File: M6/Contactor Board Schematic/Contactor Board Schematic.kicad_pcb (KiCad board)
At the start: 2 copper layers, 52.1 x 42.7 mm, 8 parts

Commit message: CT board progress
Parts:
- removed the J_EXT4 at (128.0, 112.0)
- added D2: SMCJ28A, Diode_SMD:D_SMC, F.Cu at (116.8, 113.0)
- added D4: SMCJ28A, Diode_SMD:D_SMC, F.Cu at (105.4, 105.4)
- added D5: SMCJ28CA, Diode_SMD:D_SMC, F.Cu at (105.4, 83.6)
- added D6: SMCJ28CA, Diode_SMD:D_SMC, F.Cu at (139.7, 115.6)
- added U1: 12V Buck, Converter_DCDC:Converter_DCDC_TRACO_TSR-1_THT, F.Cu at (125.8, 115.6)
- J_EXT1: footprint Connector_AMASS:AMASS_XT30PW-F_1x02_P2.50mm_Horizontal -> TerminalBlock:TerminalBlock_MaiXu_MX126-5.0-02P_1x02_P5.00mm
- J_EXT2: renamed from J_EXT5; footprint Connector_AMASS:AMASS_XT30PW-F_1x02_P2.50mm_Horizontal -> Connector_AMASS:AMASS_XT30U-M_1x02_P5.0mm_Vertical
- J_EXT3: renamed from J_EXT2; footprint Connector_AMASS:AMASS_XT30PW-F_1x02_P2.50mm_Horizontal -> Connector_AMASS:AMASS_XT30U-M_1x02_P5.0mm_Vertical
- J_EXT4: renamed from J_EXT3; footprint Connector_AMASS:AMASS_XT30PW-F_1x02_P2.50mm_Horizontal -> Connector_AMASS:AMASS_XT30U-M_1x02_P5.0mm_Vertical
- moved J_EXT1 7.52 mm to (105.4, 97.7)
- moved J_EXT2 7.33 mm to (108.5, 112.4), turned to 180 degrees
- moved J_EXT4 2.59 mm to (146.1, 98.4)
- moved J_EXT3 2.49 mm to (146.1, 87.0)
- renumbered F3 to F1
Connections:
- net /To Contactor renamed /Contactor
- J_EXT2 pad 2: /From Switch -> /Switch
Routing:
- net /Switch: track 0.00 -> 34.1 mm
- net /From Switch: track 19.8 -> 0.00 mm, vias 1 -> 0
- net /Battery +: track 19.4 -> 0.00 mm
- net /Contactor: track 36.4 -> 44.3 mm, vias 2 -> 0
- net GND: track 0.21 -> 6.69 mm
- net Net-(D2-K): track 34.3 -> 39.7 mm
- net Net-(Contactor1-Pad2): track 3.90 -> 2.70 mm
- added copper zone on B.Cu, net /Battery +
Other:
- board text added: "Main Board"
- board text added: "Motor"

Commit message: Contactor Progress
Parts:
- added H1: MountingHole_Pad, MountingHole:MountingHole_2.7mm_Pad, F.Cu at (87.4, 88.1)
- added H2: MountingHole_Pad, MountingHole:MountingHole_2.7mm_Pad, F.Cu at (87.4, 95.0)
- added H3: MountingHole_Pad, MountingHole:MountingHole_2.7mm_Pad, F.Cu at (87.4, 102.0)
- added H4: MountingHole_Pad, MountingHole:MountingHole_2.7mm_Pad, F.Cu at (87.4, 108.9)
- moved D6 1.90 mm to (139.7, 113.7)
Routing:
- net /Battery +: track 0.00 -> 11.5 mm

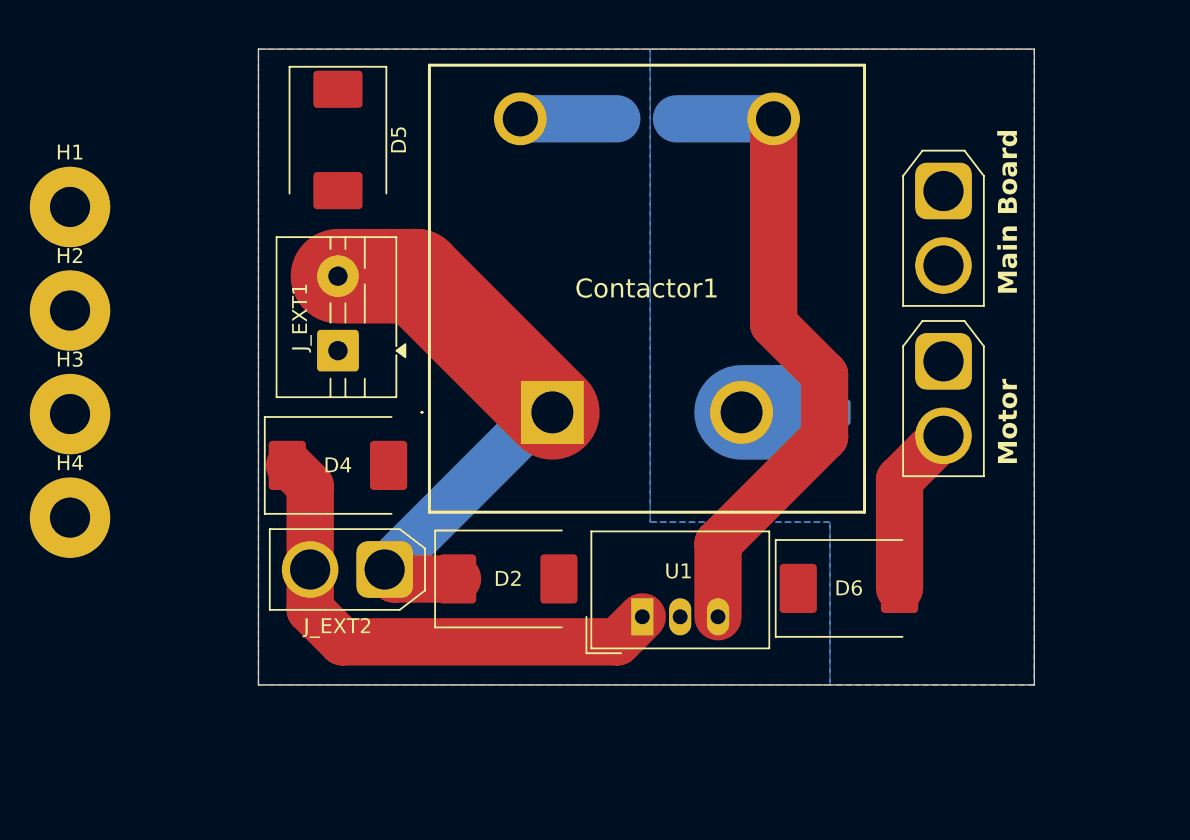
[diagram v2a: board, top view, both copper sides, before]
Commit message: XT60 connector for battery
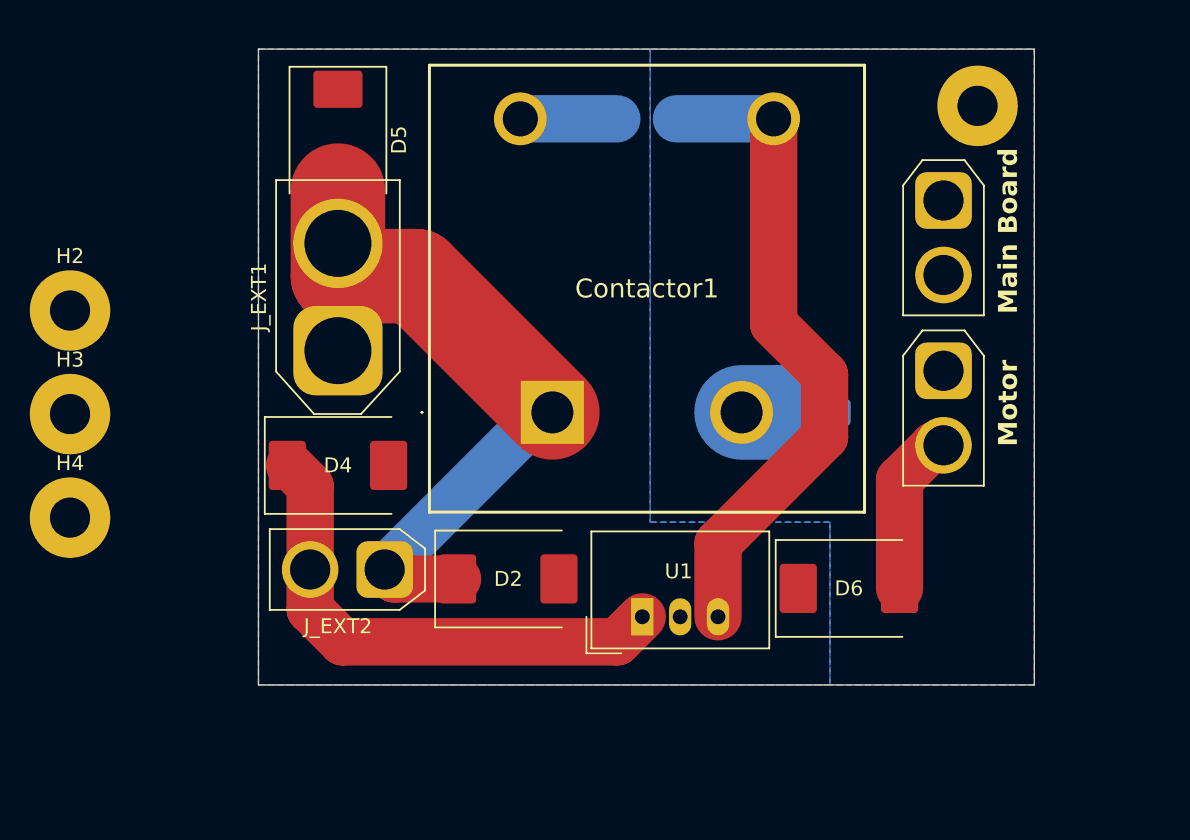
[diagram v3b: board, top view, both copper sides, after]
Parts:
- J_EXT1: footprint TerminalBlock:TerminalBlock_MaiXu_MX126-5.0-02P_1x02_P5.00mm -> Connector_AMASS:AMASS_XT60-M_1x02_P7.20mm_Vertical
- moved H1 61.3 mm to (148.3, 81.3)
- moved J_EXT4 0.64 mm to (146.1, 99.1)
- moved J_EXT3 0.63 mm to (146.1, 87.6)
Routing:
- net Net-(D2-K): track 39.7 -> 45.4 mm

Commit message: Finished contactor
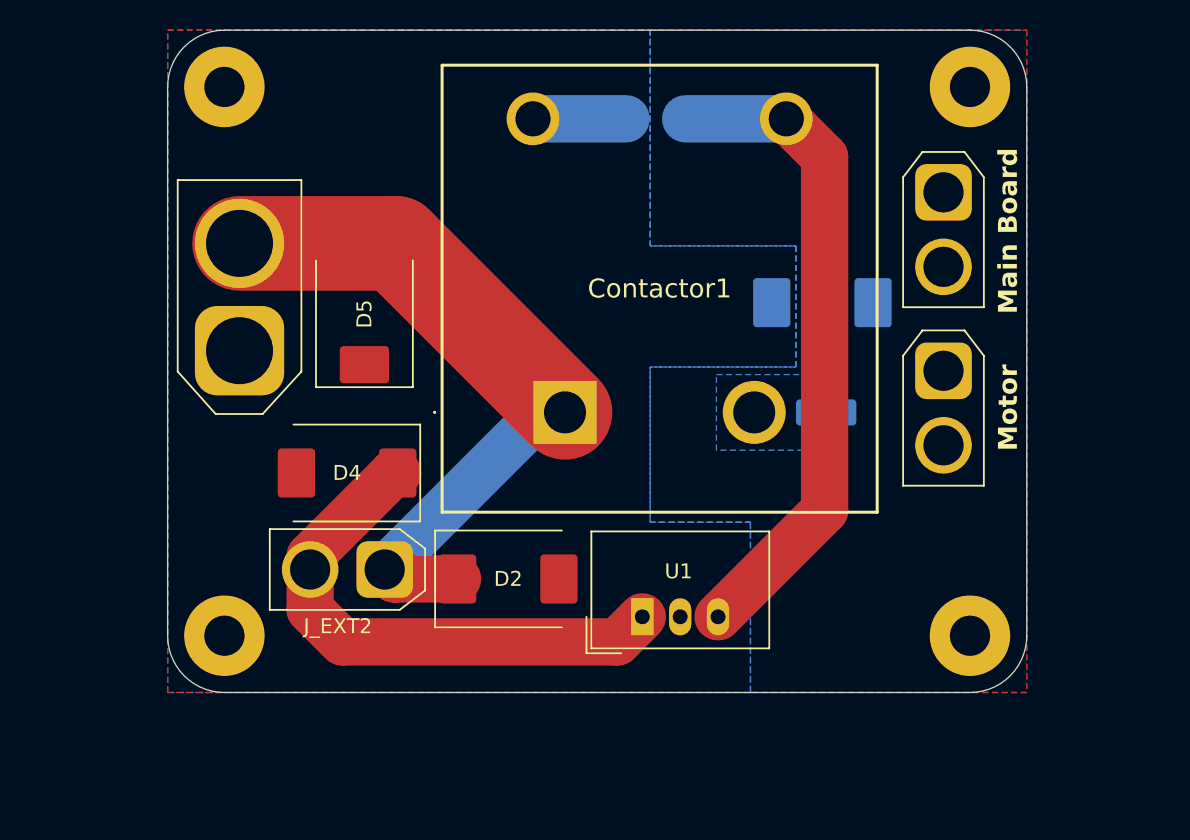
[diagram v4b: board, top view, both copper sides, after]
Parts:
- D6: moved to B.Cu
- moved H4 60.9 mm to (147.8, 116.8)
- moved D6 19.3 mm to (137.9, 94.5)
- moved H2 18.2 mm to (97.8, 80.0)
- moved H3 18.1 mm to (97.8, 116.8)
- moved D5 11.8 mm to (107.2, 95.2), turned to 90 degrees
- moved J_EXT1 6.60 mm to (98.8, 97.7)
- moved H1 1.37 mm to (147.8, 80.0)
- moved Contactor1 0.85 mm to (120.7, 101.8)
- moved D4 0.80 mm to (106.0, 105.9), turned to 180 degrees
- moved Flyback1 0.62 mm to (126.7, 82.2)
- moved J_EXT3 0.55 mm to (146.1, 87.1)
- moved F1 0.38 mm to (138.2, 101.9)
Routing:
- net /Battery +: track 11.2 -> 0.00 mm
- net Net-(D2-K): track 45.4 -> 48.9 mm
- net Net-(Contactor1-Pad2): track 2.70 -> 0.00 mm
- net /Switch: track 34.1 -> 35.7 mm
- added copper zone on B.Cu, net Net-(Contactor1-Pad2)
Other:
- board size 52.1 x 42.7 mm -> 57.7 x 44.5 mm
